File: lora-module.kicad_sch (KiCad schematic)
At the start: 6 parts, among them J101 Conn_Coaxial, Q101 PMN48XP

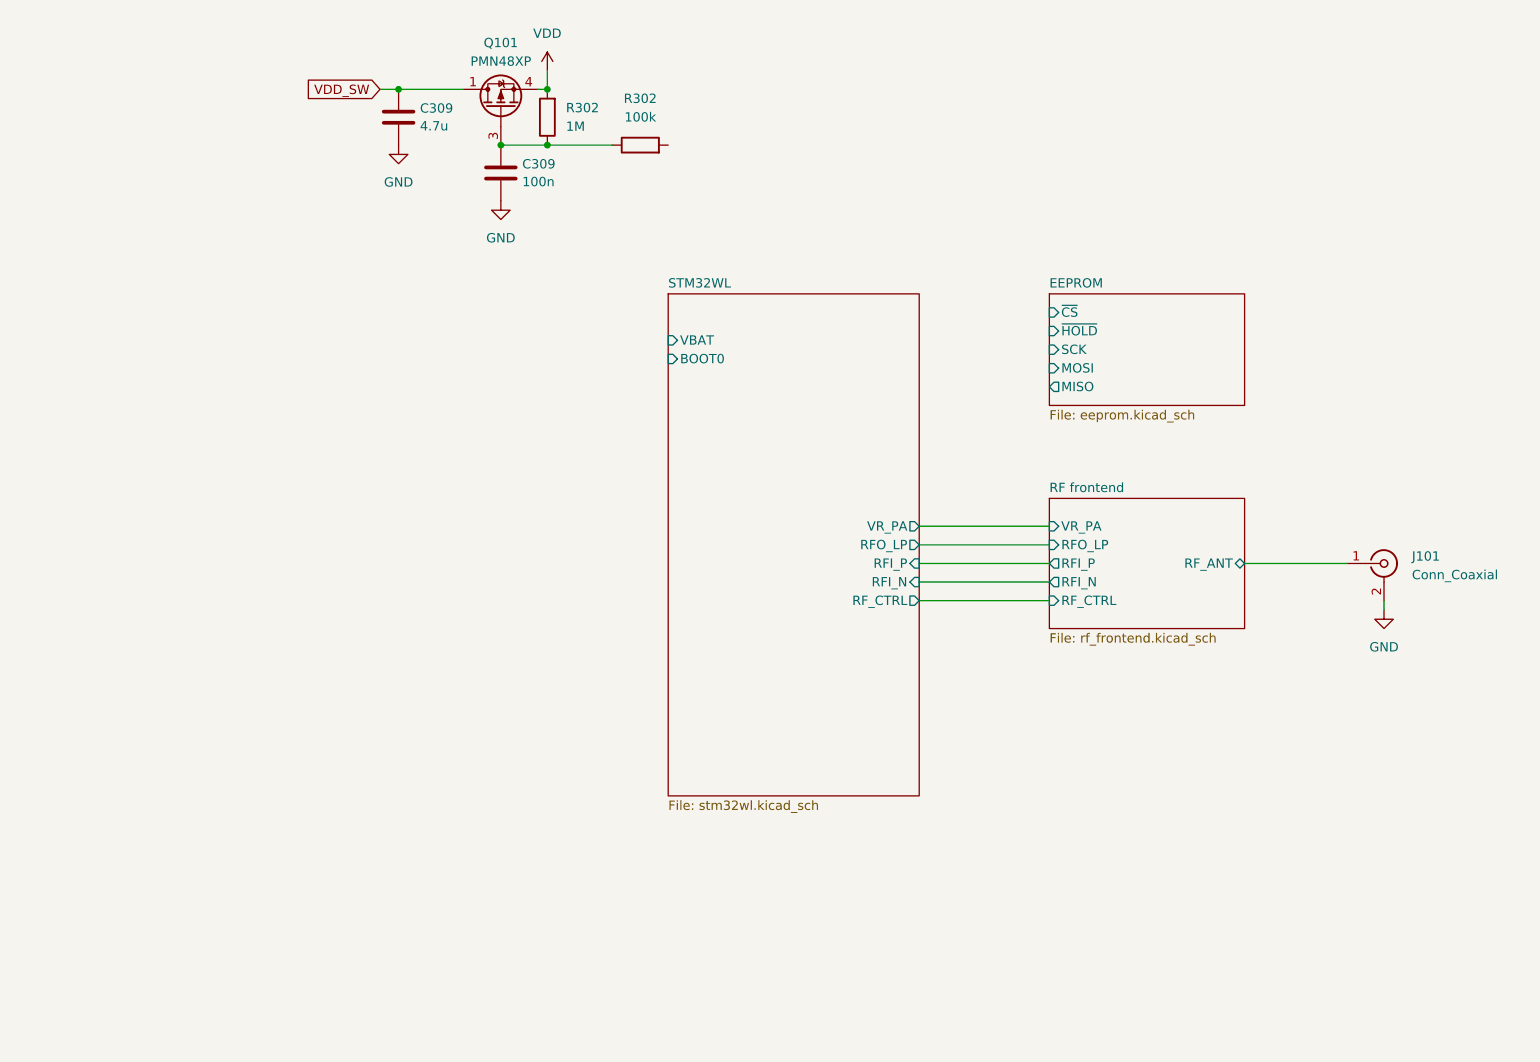
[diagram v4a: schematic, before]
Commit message: added tag-connect and a led, noticed i forgot a crystal
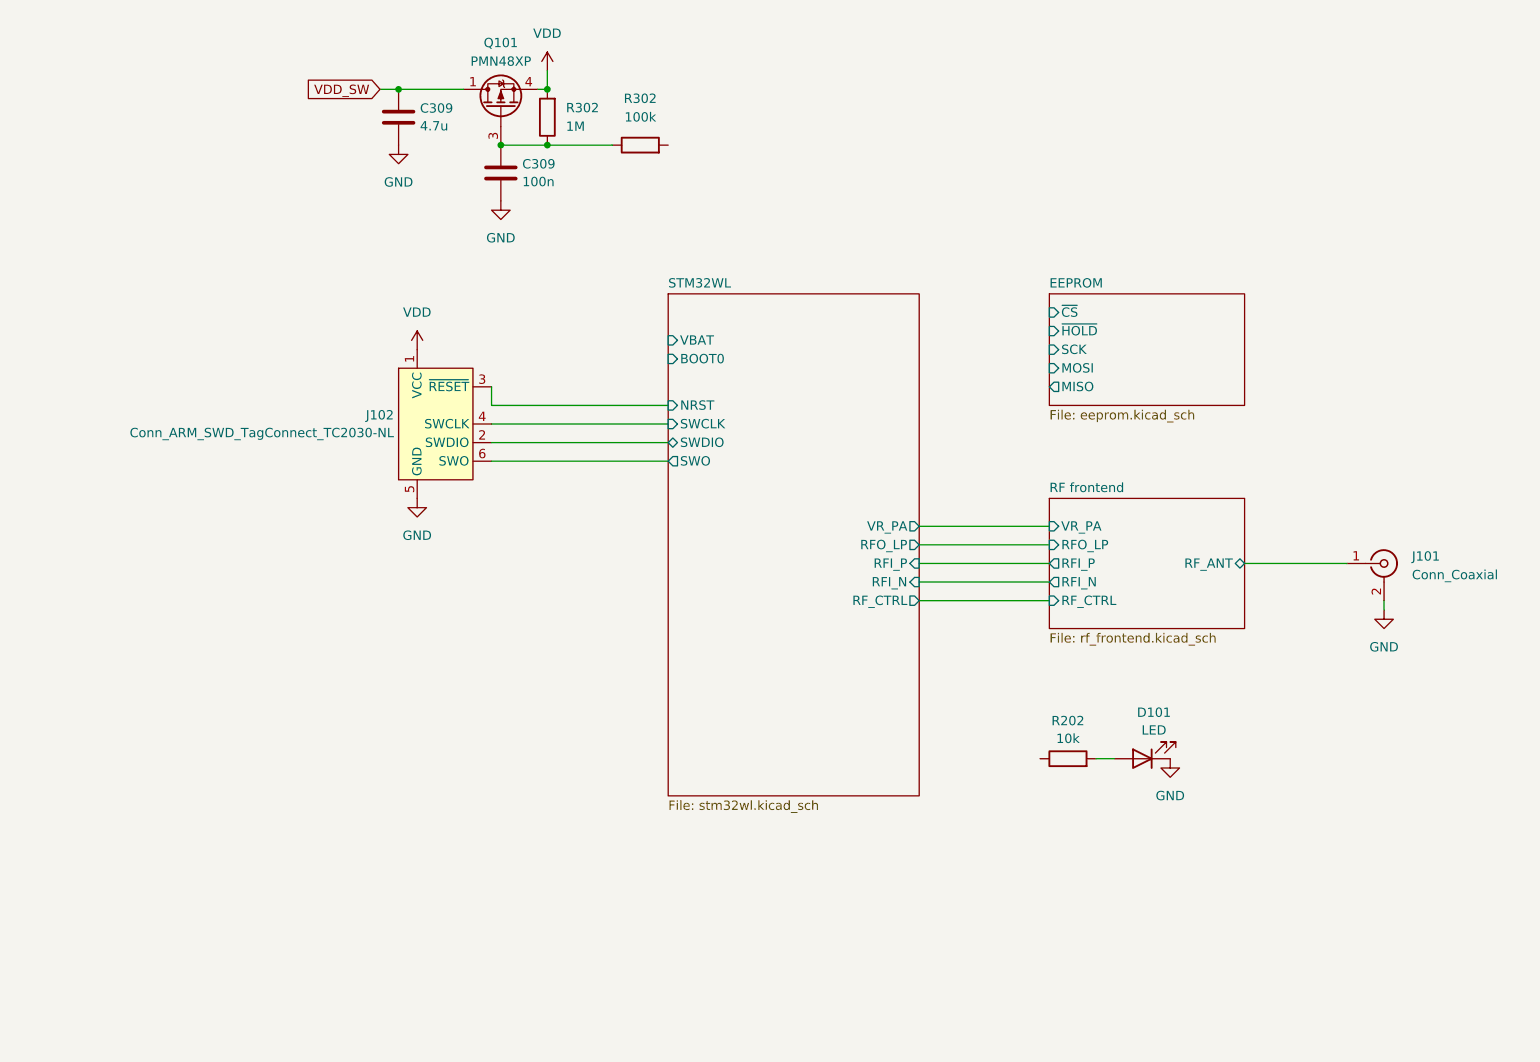
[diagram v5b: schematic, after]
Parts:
- added D101: LED, LED_SMD:LED_0402_1005Metric, symbol Device:LED
- added J102: Conn_ARM_SWD_TagConnect_TC2030-NL, Connector:Tag-Connect_TC2030-IDC-NL_2x03_P1.27mm_Vertical, symbol Connector:Conn_ARM_SWD_TagConnect_TC2030-NL
- added R202: 10k, Resistor_SMD:R_0402_1005Metric, symbol Device:R
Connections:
- net GND: now also D101.1 (K), J102.5 (GND)
- net VDD: now also J102.1 (VCC)
- new net: D101.2 (A), R202.2
- new net STM32WL/NRST: J102.3 (~{RESET})
- new net STM32WL/SWCLK: J102.4 (SWCLK)
- new net STM32WL/SWDIO: J102.2 (SWDIO)
- new net STM32WL/SWO: J102.6 (SWO)
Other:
- sheet STM32WL ports: added NRST, SWCLK, SWDIO, SWO; removed none
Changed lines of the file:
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@@
+    (stroke (width 0) (type default))
+  )
+  (wire (pts (xy 86.36 80.01) (xy 110.49 80.01))
     (stroke (width 0) (type default))
   )
@@
     (stroke (width 0) (type default))
   )
+  (wire (pts (xy 86.36 69.85) (xy 86.36 72.39))
+    (stroke (width 0) (type default))
+  )
   (wire (pts (xy 189.23 93.98) (xy 203.2 93.98))
     (stroke (width 0) (type default))
@@
     (stroke (width 0) (type default))
   )
+  (wire (pts (xy 86.36 74.93) (xy 110.49 74.93))
+    (stroke (width 0) (type default))
+  )
   (wire (pts (xy 93.98 26.67) (xy 93.98 29.21))
     (stroke (width 0) (type default))
@@
     (stroke (width 0) (type default))
   )
+  (wire (pts (xy 86.36 77.47) (xy 110.49 77.47))
+    (stroke (width 0) (type default))
+  )
+  (wire (pts (xy 86.36 72.39) (xy 110.49 72.39))
+    (stroke (width 0) (type default))
+  )
   (wire (pts (xy 144.78 96.52) (xy 162.56 96.52))
+    (stroke (width 0) (type default))
+  )
+  (wire (pts (xy 168.91 120.65) (xy 171.45 120.65))
     (stroke (width 0) (type default))
   )
@@
     )
   )
+  (symbol (lib_id "power:GND") (at 179.07 120.65 0) (unit 1)
+    (in_bom yes) (on_board yes) (dnp no) (fields_autoplaced)
+    (property "Reference" "#PWR0107" (at 179.07 127 0)
+      (effects (font (size 1.27 1.27)) hide)
+    )
+    (property "Value" "GND" (at 179.07 125.73 0)
+      (effects (font (size 1.27 1.27)))
+    )
+    (property "Footprint" "" (at 179.07 120.65 0)
+      (effects (font (size 1.27 1.27)) hide)
+    )
+    (property "Datasheet" "" (at 179.07 120.65 0)
+      (effects (font (size 1.27 1.27)) hide)
+    )
+    (pin "1")
+    (instances
+      (project "lora-module"
+        (path "/30c7e509-35af-4828-996b-9681d057624f"
+          (reference "#PWR0107") (unit 1)
+        )
+      )
+    )
+  )
+  (symbol (lib_id "power:GND") (at 76.2 85.09 0) (unit 1)
+    (in_bom yes) (on_board yes) (dnp no) (fields_autoplaced)
+    (property "Reference" "#PWR0106" (at 76.2 91.44 0)
+      (effects (font (size 1.27 1.27)) hide)
+    )
+    (property "Value" "GND" (at 76.2 90.17 0)
+      (effects (font (size 1.27 1.27)))
+    )
+    (property "Footprint" "" (at 76.2 85.09 0)
+      (effects (font (size 1.27 1.27)) hide)
+    )
+    (property "Datasheet" "" (at 76.2 85.09 0)
+      (effects (font (size 1.27 1.27)) hide)
+    )
+    (pin "1")
+    (instances
+      (project "lora-module"
+        (path "/30c7e509-35af-4828-996b-9681d057624f"
+          (reference "#PWR0106") (unit 1)
+        )
+      )
+    )
+  )
   (symbol (lib_id "Device:C") (at 73.66 33.02 0) (unit 1)
     (in_bom yes) (on_board yes) (dnp no) (fields_autoplaced)
@@
         (path "/30c7e509-35af-4828-996b-9681d057624f"
           (reference "R102") (unit 1)
+        )
+      )
+    )
+  )
+  (symbol (lib_id "power:VDD") (at 76.2 64.77 0) (unit 1)
+    (in_bom yes) (on_board yes) (dnp no) (fields_autoplaced)
+    (property "Reference" "#PWR0105" (at 76.2 68.58 0)
+      (effects (font (size 1.27 1.27)) hide)
+    )
+    (property "Value" "VDD" (at 76.2 59.69 0)
+      (effects (font (size 1.27 1.27)))
+    )
+    (property "Footprint" "" (at 76.2 64.77 0)
+      (effects (font (size 1.27 1.27)) hide)
+    )
+    (property "Datasheet" "" (at 76.2 64.77 0)
+      (effects (font (size 1.27 1.27)) hide)
+    )
+    (pin "1")
+    (instances
+      (project "lora-module"
+        (path "/30c7e509-35af-4828-996b-9681d057624f"
+          (reference "#PWR0105") (unit 1)
         )
       )
@@
     )
   )
+  (symbol (lib_id "Device:LED") (at 175.26 120.65 180) (unit 1)
+    (in_bom yes) (on_board yes) (dnp no) (fields_autoplaced)
+    (property "Reference" "D101" (at 176.8475 114.3467 0)
+      (effects (font (size 1.27 1.27)))
+    )
+    (property "Value" "LED" (at 176.8475 116.7709 0)
+      (effects (font (size 1.27 1.27)))
+    )
+    (property "Footprint" "LED_SMD:LED_0402_1005Metric" (at 175.26 120.65 0)
+      (effects (font (size 1.27 1.27)) hide)
+    )
+    (property "Datasheet" "~" (at 175.26 120.65 0)
+      (effects (font (size 1.27 1.27)) hide)
+    )
+    (pin "1")
+    (pin "2")
+    (instances
+      (project "lora-module"
+        (path "/30c7e509-35af-4828-996b-9681d057624f"
+          (reference "D101") (unit 1)
+        )
+      )
+    )
+  )
   (symbol (lib_id "power:GND") (at 73.66 36.83 0) (unit 1)
     (in_bom yes) (on_board yes) (dnp no) (fields_autoplaced)
@@
         (path "/30c7e509-35af-4828-996b-9681d057624f"
           (reference "#PWR0101") (unit 1)
+        )
+      )
+    )
+  )
+  (symbol (lib_id "Device:R") (at 165.1 120.65 90) (unit 1)
+    (in_bom yes) (on_board yes) (dnp no) (fields_autoplaced)
+    (property "Reference" "R202" (at 165.1 115.4897 90)
+      (effects (font (size 1.27 1.27)))
+    )
+    (property "Value" "10k" (at 165.1 117.9139 90)
+      (effects (font (size 1.27 1.27)))
+    )
+    (property "Footprint" "Resistor_SMD:R_0402_1005Metric" (at 165.1 122.428 90)
+      (effects (font (size 1.27 1.27)) hide)
+    )
+    (property "Datasheet" "~" (at 165.1 120.65 0)
+      (effects (font (size 1.27 1.27)) hide)
+    )
+    (pin "1")
+    (pin "2")
+    (instances
+      (project "lora-module"
+        (path "/30c7e509-35af-4828-996b-9681d057624f/93ed2c4d-2004-4e0b-a952-c18d2f9b026d"
+          (reference "R202") (unit 1)
+        )
+        (path "/30c7e509-35af-4828-996b-9681d057624f"
+          (reference "R103") (unit 1)
+        )
+      )
+    )
+  )
+  (symbol (lib_id "Connector:Conn_ARM_SWD_TagConnect_TC2030-NL") (at 78.74 74.93 0) (unit 1)
+    (in_bom no) (on_board yes) (dnp no) (fields_autoplaced)
+    (property "Reference" "J102" (at 73.025 73.7179 0)
+      (effects (font (size 1.27 1.27)) (justify right))
+    )
+    (property "Value" "Conn_ARM_SWD_TagConnect_TC2030-NL" (at 73.025 76.1421 0)
+      (effects (font (size 1.27 1.27)) (justify right))
+    )
+    (property "Footprint" "Connector:Tag-Connect_TC2030-IDC-NL_2x03_P1.27mm_Vertical" (at 78.74 92.71 0)
+      (effects (font (size 1.27 1.27)) hide)
+    )
+    (property "Datasheet" "https://www.tag-connect.com/wp-content/uploads/bsk-pdf-manager/TC2030-CTX_1.pdf" (at 78.74 90.17 0)
+      (effects (font (size 1.27 1.27)) hide)
+    )
+    (pin "1")
+    (pin "2")
+    (pin "3")
+    (pin "4")
+    (pin "5")
+    (pin "6")
+    (instances
+      (project "lora-module"
+        (path "/30c7e509-35af-4828-996b-9681d057624f"
+          (reference "J102") (unit 1)
         )
       )
@@
       (effects (font (size 1.27 1.27)) (justify left))
     )
+    (pin "NRST" input (at 110.49 72.39 180)
+      (effects (font (size 1.27 1.27)) (justify left))
+    )
+    (pin "SWCLK" input (at 110.49 74.93 180)
+      (effects (font (size 1.27 1.27)) (justify left))
+    )
+    (pin "SWDIO" bidirectional (at 110.49 77.47 180)
+      (effects (font (size 1.27 1.27)) (justify left))
+    )
+    (pin "SWO" output (at 110.49 80.01 180)
+      (effects (font (size 1.27 1.27)) (justify left))
+    )

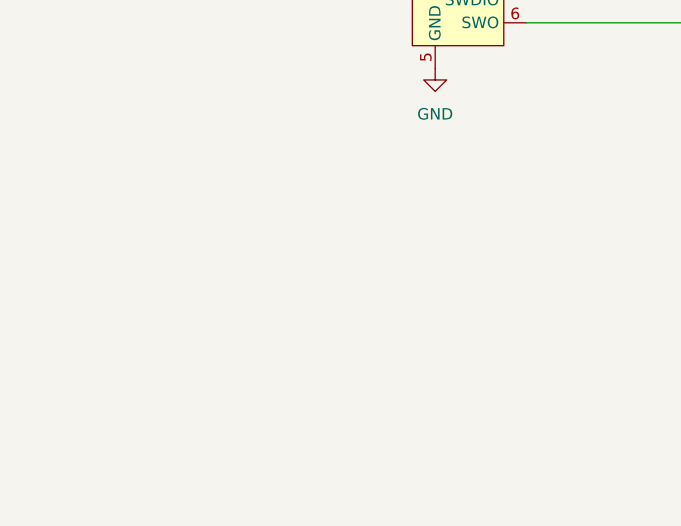
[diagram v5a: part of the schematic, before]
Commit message: added castellated edge connectors
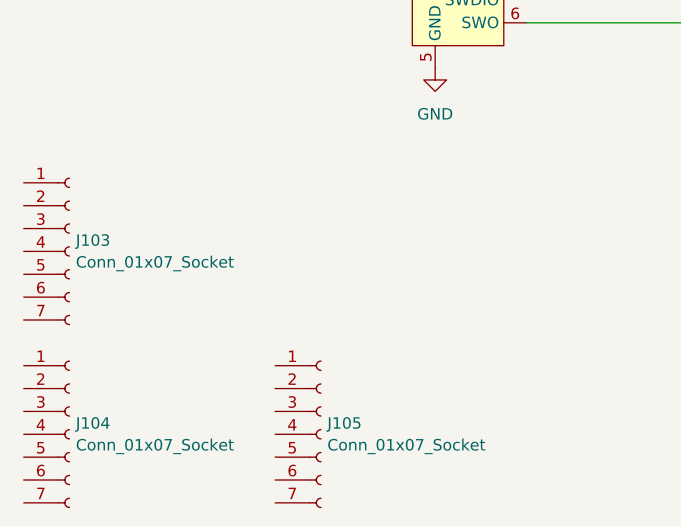
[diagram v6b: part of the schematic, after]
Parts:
- added J103, J104, J105: Conn_01x07_Socket, Connector_PinSocket_2.54mm:PinSocket_1x07_P2.54mm_Vertical, symbol Connector:Conn_01x07_Socket
